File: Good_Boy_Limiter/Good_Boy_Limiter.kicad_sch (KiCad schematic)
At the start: 48 parts, among them CN1 XT30PW-M, CN2 XT30PW-M, J1 UART, J2 Extra General Pins, Q4 AO3400A, SW3 RESET1, SW4 BOOT1, U1 ESP32-S3-WROOM-1, U6 1-178136-3, U7 LM5013DDAR

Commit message: Updated routing
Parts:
- removed D16: LED, LED_SMD:LED_0805_2012Metric_Pad1.15x1.40mm_HandSolder, symbol Device:LED
- added D19: LED, LED_SMD:LED_0805_2012Metric_Pad1.15x1.40mm_HandSolder, symbol Device:LED
- U1: LCSC Part (none) -> C2913204
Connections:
- net GND: now also D19.1 (K); no longer R33.1
- net GPIO38: now also R13.1
- net GPIO6: no longer R13.1
- net at D11.2 (A), Q4.3 (D), U6.2: now also R33.2
- new net: D19.2 (A), R33.1
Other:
- sheet In-rush controller ports: added GPIO; removed none
- moved on the sheet: R33
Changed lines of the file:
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@@
 	(title_block
 		(title "GBL (Good Boy Limiter)")
-		(date "2026-04-15")
+		(date "2026-05-01")
 	)
 	(rectangle
@@
 	)
 	(junction
-		(at 269.24 63.5)
-		(diameter 0)
-		(color 0 0 0 0)
-	)
-	(junction
 		(at 185.42 25.4)
 		(diameter 0)
@@
 	)
 	(junction
+		(at 269.24 38.1)
+		(diameter 0)
+		(color 0 0 0 0)
+	)
+	(junction
 		(at 50.8 115.57)
 		(diameter 0)
@@
 	)
 	(junction
-		(at 269.24 71.12)
-		(diameter 0)
-		(color 0 0 0 0)
-	)
-	(junction
 		(at 185.42 31.75)
 		(diameter 0)
@@
 	(wire
 		(pts
-			(xy 269.24 71.12) (xy 269.24 72.39)
+			(xy 269.24 54.61) (xy 269.24 72.39)
 		)
 		(stroke
@@
 	(wire
 		(pts
-			(xy 269.24 63.5) (xy 271.78 63.5)
-		)
-		(stroke
-			(width 0)
-			(type default)
-		)
-	)
-	(wire
-		(pts
 			(xy 120.65 33.02) (xy 120.65 41.91)
 		)
@@
 	(wire
 		(pts
-			(xy 269.24 63.5) (xy 269.24 71.12)
-		)
-		(stroke
-			(width 0)
-			(type default)
-		)
-	)
-	(wire
-		(pts
 			(xy 43.18 59.69) (xy 48.26 59.69)
 		)
@@
 	(wire
 		(pts
-			(xy 269.24 34.29) (xy 269.24 39.37)
+			(xy 269.24 34.29) (xy 269.24 38.1)
 		)
 		(stroke
@@
 	(wire
 		(pts
-			(xy 269.24 63.5) (xy 269.24 54.61)
-		)
-		(stroke
-			(width 0)
-			(type default)
-		)
-	)
-	(wire
-		(pts
 			(xy 220.98 46.99) (xy 214.63 46.99)
 		)
@@
 	(wire
 		(pts
-			(xy 276.86 71.12) (xy 269.24 71.12)
-		)
-		(stroke
-			(width 0)
-			(type default)
-		)
-	)
-	(wire
-		(pts
 			(xy 127 73.66) (xy 127 74.93)
 		)
@@
 	(wire
 		(pts
+			(xy 269.24 38.1) (xy 269.24 39.37)
+		)
+		(stroke
+			(width 0)
+			(type default)
+		)
+	)
+	(wire
+		(pts
 			(xy 34.29 109.22) (xy 36.83 109.22)
 		)
@@
 	(wire
 		(pts
+			(xy 38.1 43.18) (xy 46.99 43.18)
+		)
+		(stroke
+			(width 0)
+			(type default)
+		)
+	)
+	(wire
+		(pts
 			(xy 55.88 187.96) (xy 55.88 185.42)
 		)
@@
 		)
 	)
-	(label "GPIO6"
+	(label "GPIO38"
 		(at 251.46 44.45 180)
 		(effects
@@
 		)
 	)
+	(label "GPIO2"
+		(at 46.99 43.18 180)
+		(effects
+			(font
+				(size 1.27 1.27)
+			)
+			(justify right bottom)
+		)
+	)
 	(label "5VUSB"
 		(at 157.48 111.76 0)
@@
 	(symbol
 		(lib_id "Device:LED")
-		(at 276.86 67.31 90)
+		(at 260.35 38.1 0)
 		(unit 1)
 		(exclude_from_sim no)
@@
 		(on_board yes)
 		(dnp no)
-		(fields_autoplaced yes)
-		(property "Reference" "D16"
-			(at 280.67 67.6274 90)
+		(property "Reference" "D19"
+			(at 260.35 35.306 0)
 			(effects
 				(font
 					(size 1.27 1.27)
 				)
-				(justify right)
 			)
 		)
 		(property "Value" "LED"
-			(at 280.67 70.1674 90)
+			(at 260.604 40.894 0)
 			(effects
 				(font
 					(size 1.27 1.27)
 				)
-				(justify right)
 			)
 		)
 		(property "Footprint" "LED_SMD:LED_0805_2012Metric_Pad1.15x1.40mm_HandSolder"
-			(at 276.86 67.31 0)
+			(at 260.35 38.1 0)
 			(effects
 				(font
@@
 		)
 		(property "Datasheet" "~"
-			(at 276.86 67.31 0)
+			(at 260.35 38.1 0)
 			(effects
 				(font
@@
 		)
 		(property "Description" "Light emitting diode"
-			(at 276.86 67.31 0)
+			(at 260.35 38.1 0)
 			(effects
 				(font
@@
 		)
 		(property "Sim.Pins" "1=K 2=A"
-			(at 276.86 67.31 0)
+			(at 260.35 38.1 0)
 			(effects
 				(font
@@
 		)
 		(property "LCSC Part" "C2297"
-			(at 276.86 67.31 0)
+			(at 260.35 38.1 0)
 			(effects
 				(font
@@
 		)
 		(property "Sim.Device" ""
-			(at 276.86 67.31 0)
+			(at 260.35 38.1 0)
 			(effects
 				(font
@@
 		)
 		(property "Sim.Type" ""
-			(at 276.86 67.31 0)
+			(at 260.35 38.1 0)
 			(effects
 				(font
@@
 			(project "Good_Boy_Limiter"
 				(path "/e6249df1-5b78-4b75-b804-4c6c30b1afc2"
-					(reference "D16")
+					(reference "D19")
 					(unit 1)
 				)
@@
 	(symbol
 		(lib_id "Device:R_Small")
-		(at 274.32 63.5 90)
+		(at 266.7 38.1 90)
 		(unit 1)
 		(exclude_from_sim no)
@@
 		(fields_autoplaced yes)
 		(property "Reference" "R33"
-			(at 274.32 58.42 90)
+			(at 266.7 33.02 90)
 			(effects
 				(font
@@
 		)
 		(property "Value" "1k"
-			(at 274.32 60.96 90)
+			(at 266.7 35.56 90)
 			(effects
 				(font
@@
 		)
 		(property "Footprint" "Resistor_SMD:R_0402_1005Metric"
-			(at 274.32 63.5 0)
+			(at 266.7 38.1 0)
 			(effects
 				(font
@@
 		)
 		(property "Datasheet" "~"
-			(at 274.32 63.5 0)
+			(at 266.7 38.1 0)
 			(effects
 				(font
@@
 		)
 		(property "Description" "Resistor, small symbol"
-			(at 274.32 63.5 0)
+			(at 266.7 38.1 0)
 			(effects
 				(font
@@
 		)
 		(property "LCSC Part" "C173697"
-			(at 274.32 63.5 0)
+			(at 266.7 38.1 0)
 			(effects
 				(font
@@
 			)
 		)
+		(property "LCSC Part" "C2913204"
+			(at 185.42 59.69 0)
+			(effects
+				(font
+					(size 1.27 1.27)
+				)
+				(hide yes)
+			)
+		)
 		(pin "4"
 		)
@@
 	(symbol
 		(lib_id "power:GND")
+		(at 256.54 38.1 270)
+		(unit 1)
+		(exclude_from_sim no)
+		(in_bom yes)
+		(on_board yes)
+		(dnp no)
+		(property "Reference" "#PWR065"
+			(at 250.19 38.1 0)
+			(effects
+				(font
+					(size 1.27 1.27)
+				)
+				(hide yes)
+			)
+		)
+		(property "Value" "GND"
+			(at 252.73 38.0999 90)
+			(effects
+				(font
+					(size 1.27 1.27)
+				)
+				(justify right)
+			)
+		)
+		(property "Footprint" ""
+			(at 256.54 38.1 0)
+			(effects
+				(font
+					(size 1.27 1.27)
+				)
+				(hide yes)
+			)
+		)
+		(property "Datasheet" ""
+			(at 256.54 38.1 0)
+			(effects
+				(font
+					(size 1.27 1.27)
+				)
+				(hide yes)
+			)
+		)
+		(property "Description" "Power symbol creates a global label with name \"GND\" , ground"
+			(at 256.54 38.1 0)
+			(effects
+				(font
+					(size 1.27 1.27)
+				)
+				(hide yes)
+			)
+		)
+		(pin "1"
+		)
+		(instances
+			(project "Good_Boy_Limiter"
+				(path "/e6249df1-5b78-4b75-b804-4c6c30b1afc2"
+					(reference "#PWR065")
+					(unit 1)
+				)
+			)
+		)
+	)
+	(symbol
+		(lib_id "power:GND")
 		(at 86.36 180.34 0)
 		(unit 1)
@@
 			(effects
 				(font
+					(size 1.27 1.27)
+				)
+				(justify right)
+			)
+		)
+		(pin "GPIO" input
+			(at 38.1 43.18 0)
+			(effects
+				(font

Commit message: routing finished
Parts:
- removed J1: UART, Connector_PinHeader_2.54mm:PinHeader_1x03_P2.54mm_Vertical, symbol Connector_Generic:Conn_01x03
- added TP10: GND, TestPoint:TestPoint_Pad_D2.0mm, symbol Connector:TestPoint
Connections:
- net GND: now also J2.2 (Pin_2), J2.4 (Pin_4), J2.6 (Pin_6), TP10.1; no longer J2.7 (Pin_7), J2.9 (Pin_9)
- net GPIO1: now also J2.9 (Pin_9)
- net GPIO15: no longer J2.4 (Pin_4)
- net GPIO16: no longer J2.6 (Pin_6)
- net GPIO7: no longer J2.3 (Pin_3)
- net RX: now also J2.3 (Pin_3)
- net SCL: now also J2.7 (Pin_7); no longer J2.2 (Pin_2)
- net SDA: now also J2.5 (Pin_5); no longer J2.1 (Pin_1)
- net TX: now also J2.1 (Pin_1)
- net GPIO3: no longer names the net of U1.15 (IO3)
- no-connect marks 8 -> 9

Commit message: DRC fixes
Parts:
- removed U6: 1-178136-3, easyeda2kicad:1-178136-3_TYC, symbol easyeda2kicad:1-178136-3
- added U2: 1-178136-3, 1-178136-3_TYC, symbol easyeda2kicad:1-178136-3
- C3, C4: footprint Capacitor_SMD:C_0201_0603Metric_Pad0.64x0.40mm_HandSolder -> Capacitor_SMD:C_0603_1608Metric
- R26: footprint Resistor_SMD:R_0201_0603Metric_Pad0.64x0.40mm_HandSolder -> Resistor_SMD:R_0603_1608Metric
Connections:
- net +12V: now also U2.3
- net GND: now also U2.4, U2.5
- net at D11.2 (A), Q4.3 (D), R33.2: now also U2.2
- net GPIO10: no longer names the net of U1.18 (IO10)
- net GPIO11: no longer names the net of U1.19 (IO11)
- net GPIO12: no longer names the net of U1.20 (IO12)
- net GPIO13: no longer names the net of U1.21 (IO13)
- net GPIO14: no longer names the net of U1.22 (IO14)
- net GPIO16: no longer names the net of U1.9 (IO16)
- net GPIO18: no longer names the net of U1.11 (IO18)
- net GPIO39: no longer names the net of U1.32 (IO39)
- net GPIO40: no longer names the net of U1.33 (IO40)
- net GPIO41: no longer names the net of U1.34 (IO41)
- net GPIO42: no longer names the net of U1.35 (IO42)
- net GPIO47: no longer names the net of U1.24 (IO47)
- net GPIO48: no longer names the net of U1.25 (IO48)
- net GPIO5: no longer names the net of U1.5 (IO5)
- net GPIO7: no longer names the net of U1.7 (IO7)
- no-connect marks 9 -> 24
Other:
- moved on the sheet: D19, Q4, R13, R26, R33

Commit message: Added pictures and title page
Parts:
- renumbered R3 to Rpre1
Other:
- note added: "Relay connector with low-side transistor"
- moved on the sheet: C3, C4, C5, C6, D11, D17, D19, H1, H2, H3, H4, J2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

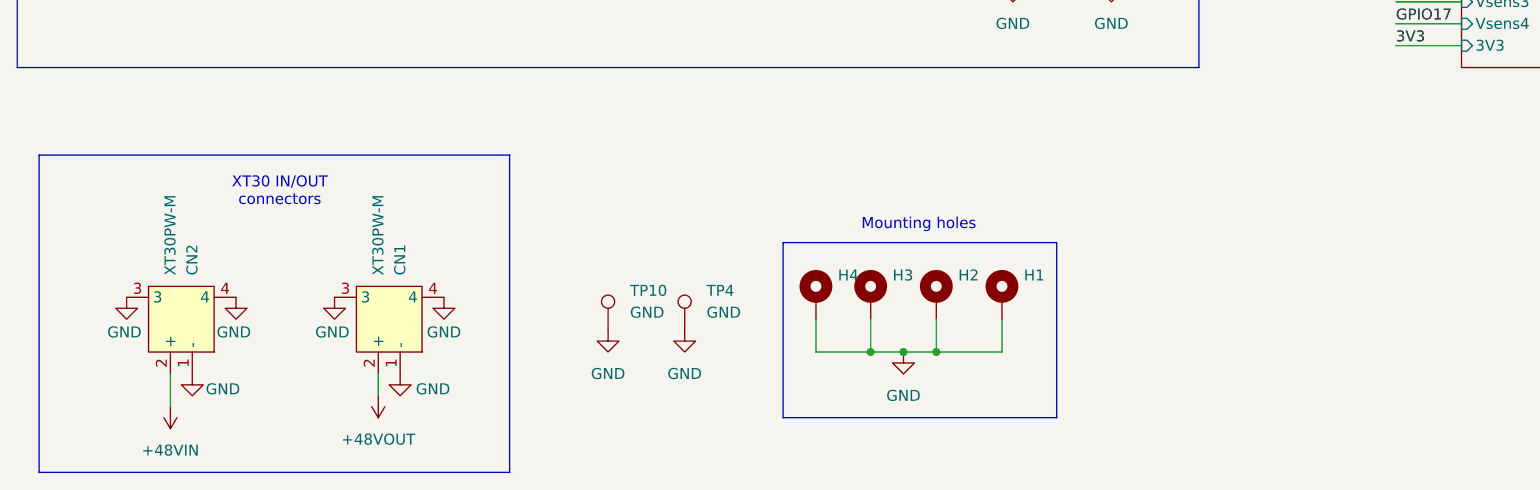
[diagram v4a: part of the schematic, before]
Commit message: added 3Ds and added more output fore PDBs
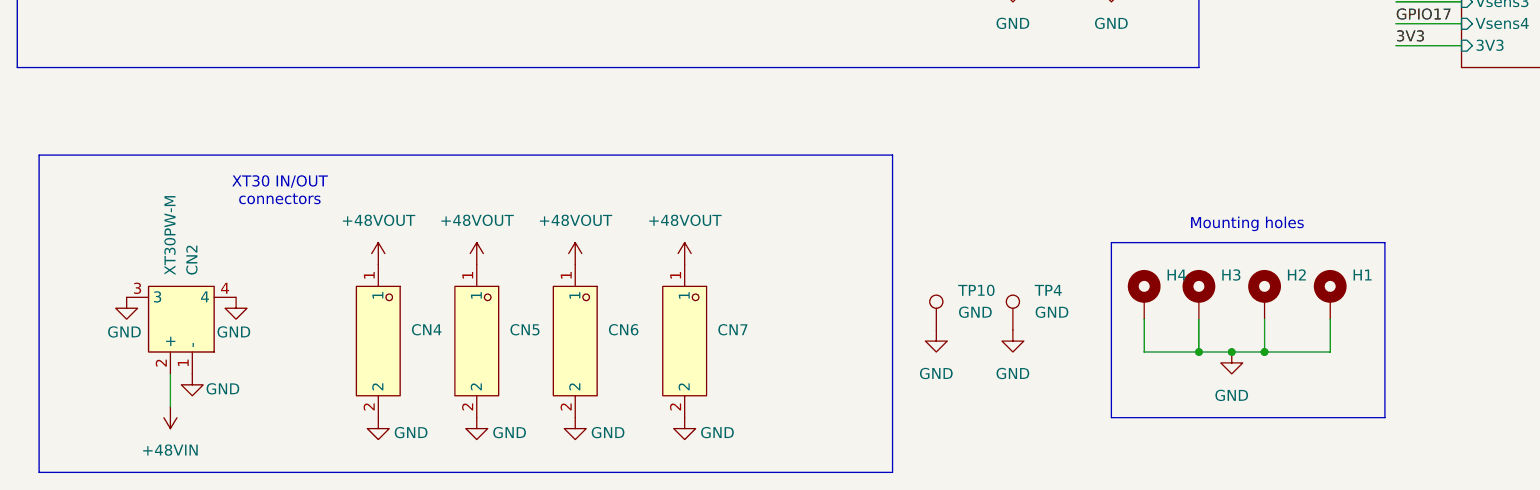
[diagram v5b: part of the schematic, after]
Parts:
- removed CN1: XT30PW-M, easyeda2kicad:CONN-TH_XT30PW-M, symbol easyeda2kicad:XT30PW-M
- added CN4, CN5, CN6, CN7: XT30UW-F.G.Y, easyeda2kicad:CONN-TH_XT30UW-F.G.Y, symbol easyeda2kicad:XT30UW-F.G.Y
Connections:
- net +48VOUT: now also CN4.1, CN5.1, CN6.1, CN7.1
- net GND: now also CN4.2, CN5.2, CN6.2, CN7.2
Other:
- moved on the sheet: H1, H2, H3, H4, TP10, TP4
